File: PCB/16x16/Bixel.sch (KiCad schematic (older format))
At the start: 263 parts, among them J1 Conn_01x12, J2 Conn_01x12, J3 Screw_Terminal_01x02, U1 74HC595, U2 74HC595

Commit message: More work on PCB Layout.
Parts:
- added J4: Screw_Terminal_01x02, TerminalBlocks_Phoenix:TerminalBlock_Phoenix_MPT-2.54mm_2pol, symbol Screw_Terminal_01x02
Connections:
- net +5V: no longer B1.1 (VCC), B144.5 (VCC), B160.8 (VCC), B176.5 (VCC), B192.8 (VCC), B208.5 (VCC), B224.8 (VCC), B240.5 (VCC), B256.8 (VCC)
- net GND: now also J4.1 (Pin_1), J4.2 (Pin_2); no longer J3.2 (Pin_2)
- new net +5VL: B144.5 (VCC), B160.8 (VCC), B176.5 (VCC), B192.8 (VCC), B208.5 (VCC), B224.8 (VCC), B240.5 (VCC), B256.8 (VCC), J3.2 (Pin_2)
- no-connect marks 6 -> 7

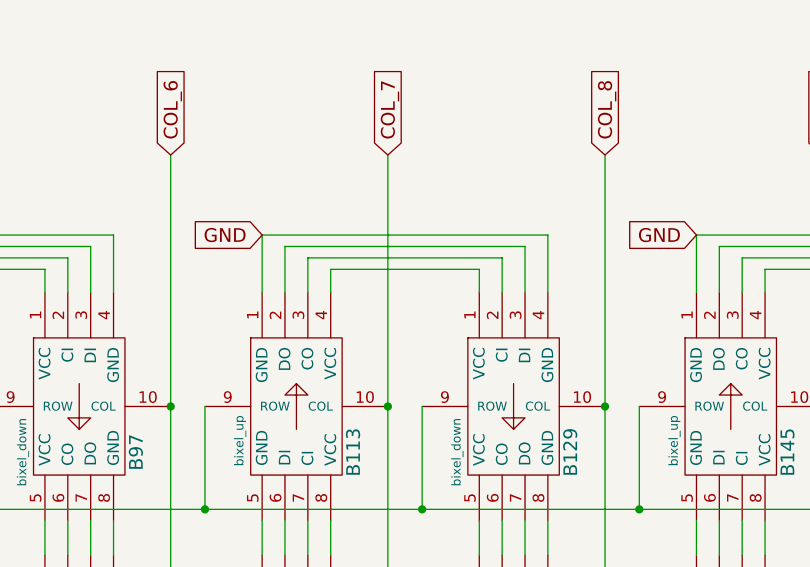
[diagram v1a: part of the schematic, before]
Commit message: Initial draft of layout complete.
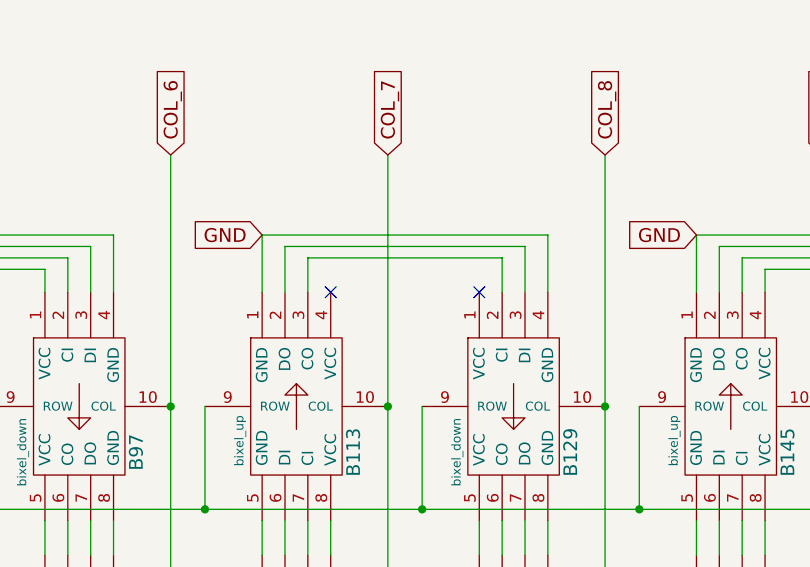
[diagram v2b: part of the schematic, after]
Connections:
- net at B113.4 (VCC): no longer B129.1 (VCC)
- no-connect marks 7 -> 9
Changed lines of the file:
@@
 	15500 2300 15500 2450
-Wire Wire Line
-	14750 2450 14750 2350
-Wire Wire Line
-	14750 2350 15400 2350
-Wire Wire Line
-	15400 2350 15400 2450
 Wire Wire Line
 	16350 2450 16350 2200
@@
 	-1   0    0    1
 $EndComp
+NoConn ~ 15400 2450
+NoConn ~ 14750 2450
 $EndSCHEMATC

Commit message: Changed screw terminal footprint to 3.5mm pitch
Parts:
- J3, J4: footprint TerminalBlocks_Phoenix:TerminalBlock_Phoenix_MPT-2.54mm_2pol -> TerminalBlocks_Phoenix:TerminalBlock_Phoenix_PT-3.5mm_2pol
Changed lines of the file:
@@
 F 0 "J3" H 25900 5550 50  0000 C CNN
 F 1 "Screw_Terminal_01x02" V 26050 5400 50  0000 C CNN
-F 2 "TerminalBlocks_Phoenix:TerminalBlock_Phoenix_MPT-2.54mm_2pol" H 25900 5450 50  0001 C CNN
+F 2 "TerminalBlocks_Phoenix:TerminalBlock_Phoenix_PT-3.5mm_2pol" H 25900 5450 50  0001 C CNN
 F 3 "" H 25900 5450 50  0001 C CNN
 	1    25900 5450
@@
 F 0 "J4" H 26800 5550 50  0000 C CNN
 F 1 "Screw_Terminal_01x02" V 26950 5400 50  0000 C CNN
-F 2 "TerminalBlocks_Phoenix:TerminalBlock_Phoenix_MPT-2.54mm_2pol" H 26800 5450 50  0001 C CNN
+F 2 "TerminalBlocks_Phoenix:TerminalBlock_Phoenix_PT-3.5mm_2pol" H 26800 5450 50  0001 C CNN
 F 3 "" H 26800 5450 50  0001 C CNN
 	1    26800 5450
@@
 	25700 5550 25700 5700
 $Comp
-L +5VL #PWR?
+L +5VL #PWR03
 U 1 1 5B4E592B
 P 25700 5700
-F 0 "#PWR?" H 25700 5550 50  0001 C CNN
+F 0 "#PWR03" H 25700 5550 50  0001 C CNN
 F 1 "+5VL" H 25700 5840 50  0000 C CNN
 F 2 "" H 25700 5700 50  0001 C CNN
